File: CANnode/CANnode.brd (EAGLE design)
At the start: 57.9 x 57.7 mm, 247 parts, among them IC1 ISO1050DUB, IC2 ISO1050DUB, Q1 FDV302P, Q3 FDV302P, U1 LM324PW, U10 FT2232HL, U11 93LC56C-I/SN, U2 TPS70445_PWP_24, U3 LM324PW, U4 LM324PW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

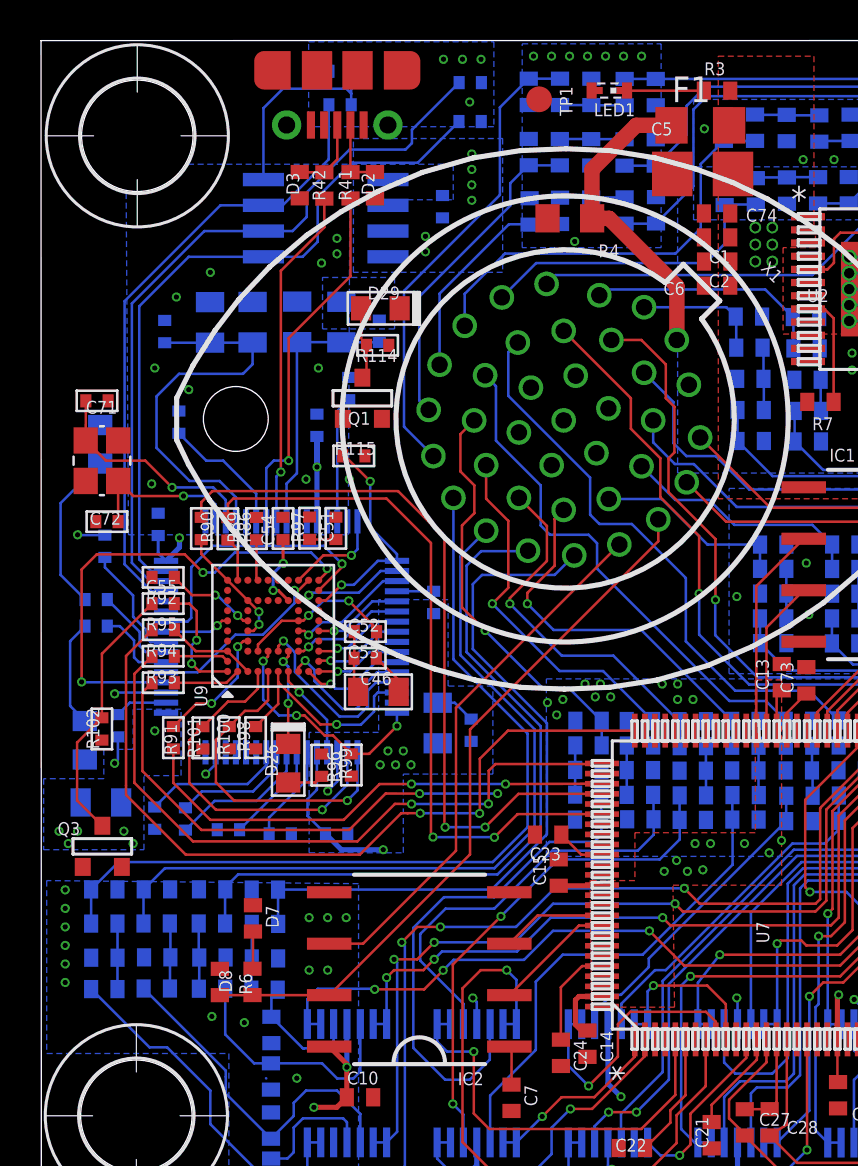
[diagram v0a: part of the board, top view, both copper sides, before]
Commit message: Finished routing bottom layer
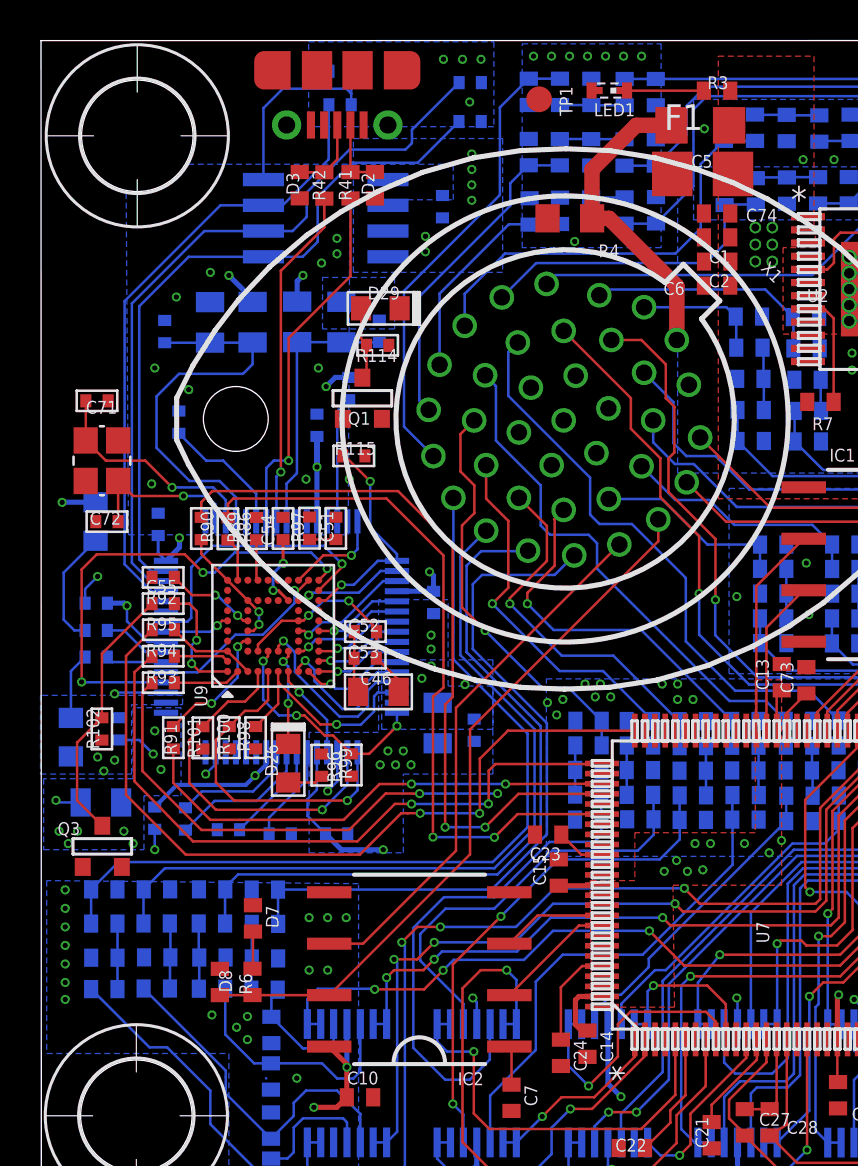
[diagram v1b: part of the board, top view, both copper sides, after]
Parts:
- moved D28 3.82 mm to (10.5, 46.3)
- moved C64 2.84 mm to (10.7, 42.3), turned to 0 degrees
- moved R106 1.52 mm to (10.7, 39.7)
- moved R107 1.52 mm to (10.7, 41.0)
- moved D27 0.70 mm to (9.53, 35.8)
- moved C67 0.17 mm to (11.8, 36.1)
- moved C65 0.15 mm to (29.3, 36.1)
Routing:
- net GND: track 24.4 -> 27.4 mm, vias 95 -> 102
- net N$43: track 8.02 -> 5.82 mm
- net N$42: track 5.30 -> 3.29 mm
- net N$25: track 4.12 -> 3.00 mm
- net N$26: track 4.37 -> 3.34 mm
- net +3V3: track 64.2 -> 65.1 mm, vias 26 -> 39
- net +1V8: vias 11 -> 12

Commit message: Finished grounding and powering. Whole board needs to be reviewed
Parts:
- moved R97 3.05 mm to (24.3, 46.0)
- moved D25 2.55 mm to (57.1, 46.2), turned to 90 degrees
- moved R5 2.43 mm to (57.1, 43.6), turned to 90 degrees
- moved C52 1.77 mm to (25.0, 42.3), turned to 0 degrees
- moved C53 1.56 mm to (25.0, 40.8), turned to 0 degrees
- moved C25 1.39 mm to (53.2, 21.8)
- moved C15 0.89 mm to (33.2, 28.2)
- moved C17 0.78 mm to (54.4, 24.9)
- moved C16 0.76 mm to (48.1, 18.1)
- moved C18 0.76 mm to (53.5, 23.6)
- moved C20 0.75 mm to (53.7, 27.8)
- moved R102 0.70 mm to (10.5, 36.7)
- moved C46 0.57 mm to (24.0, 38.0), turned to 270 degrees
- moved R7 0.37 mm to (46.7, 52.5), turned to 270 degrees
- moved C24 0.25 mm to (33.4, 20.1)
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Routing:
- net GND: track 27.4 -> 95.6 mm, vias 102 -> 137
- net +5V: track 20.3 -> 40.4 mm
- net +3V3: track 65.1 -> 82.9 mm, vias 39 -> 59
- net A3_3V3: track 13.9 -> 20.3 mm
- net POWERGOOD: track 1.30 -> 5.48 mm
- net CAN2L: track 28.5 -> 32.5 mm
- net CAN1L: track 20.1 -> 22.7 mm
- net +1V2: track 12.3 -> 13.8 mm
- net D4_BUFFERED: track 13.9 -> 14.9 mm
- net A11_3V3: track 46.4 -> 47.2 mm
- net A14_BUFFERED: track 19.2 -> 18.4 mm
- net N$12: track 5.59 -> 4.85 mm
- added copper zone on layer 1, net GND

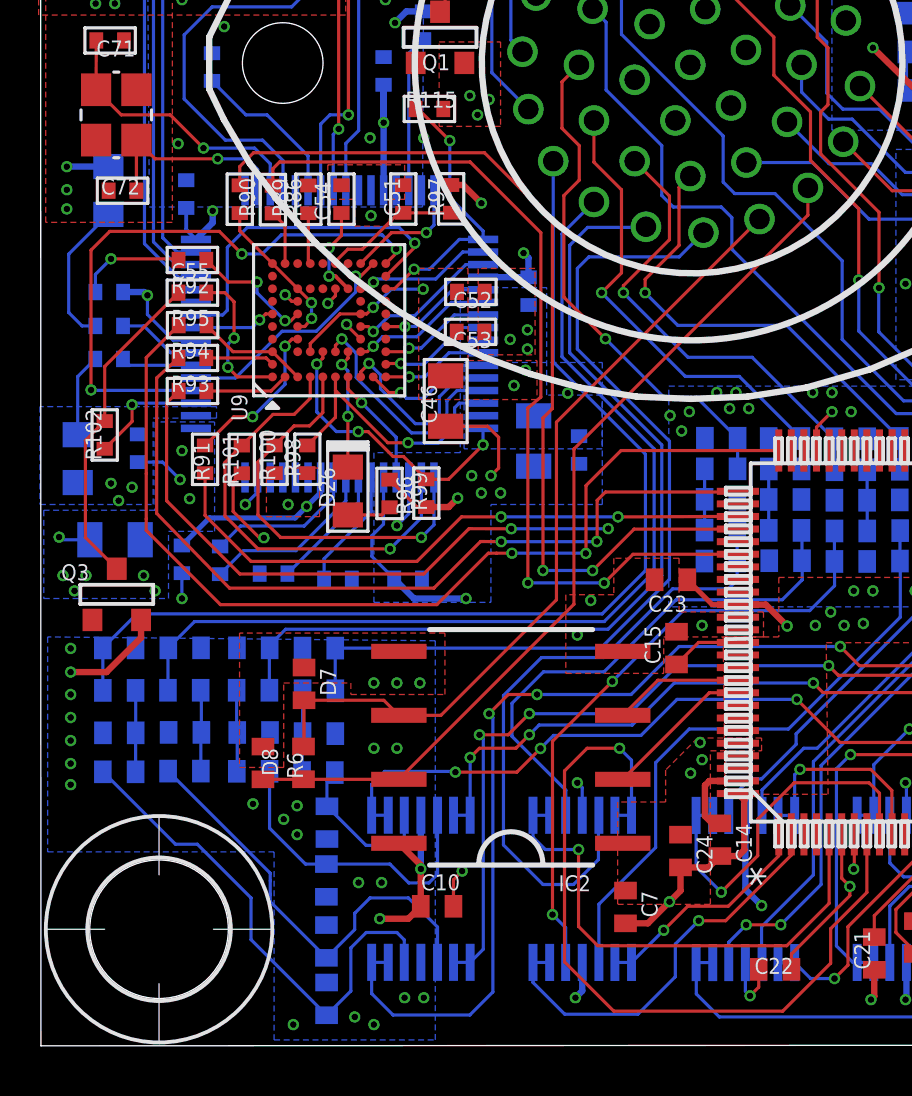
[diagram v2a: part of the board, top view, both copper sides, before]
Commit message: Routed missing JTAG to MCU connections
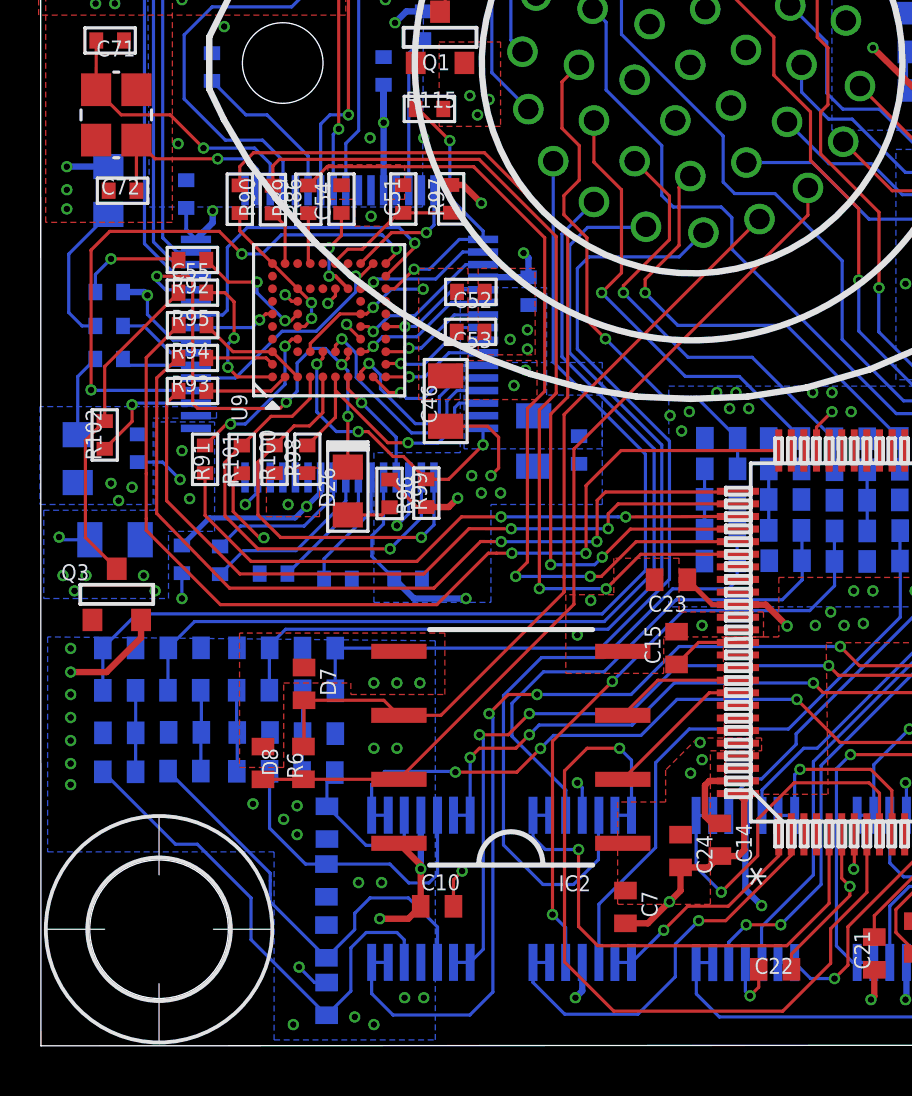
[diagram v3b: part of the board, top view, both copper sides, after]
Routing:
- net MCU_RTCK: track 0.00 -> 34.2 mm, vias 0 -> 2
- net POWER_EN: track 4.79 -> 20.9 mm, vias 2 -> 4
- net MCU_TDI: track 24.1 -> 30.0 mm
- net GND: track 95.6 -> 97.0 mm, vias 137 -> 138
- net MCU_RESET: track 35.5 -> 36.1 mm
- net +3V3: vias 59 -> 58

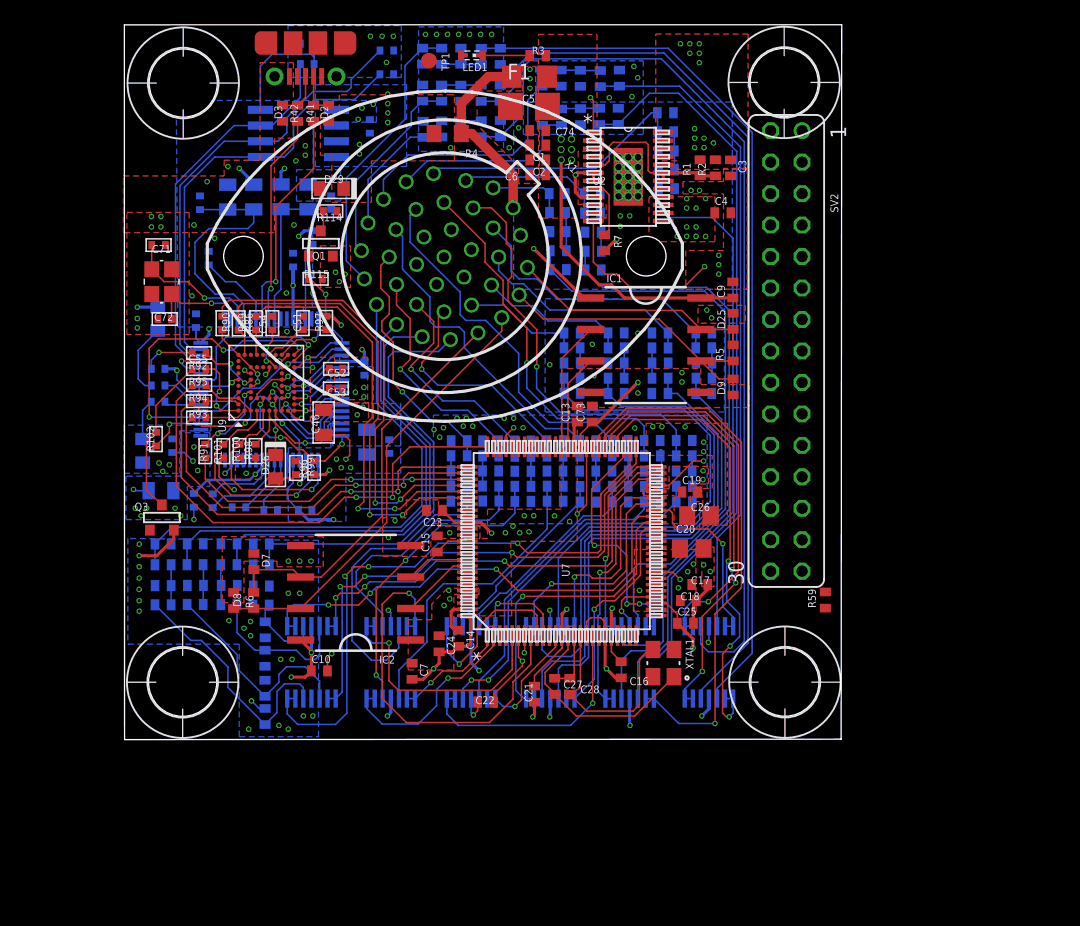
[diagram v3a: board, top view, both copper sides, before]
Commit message: Changed mounting holes to big vias. Move the origin of the board.
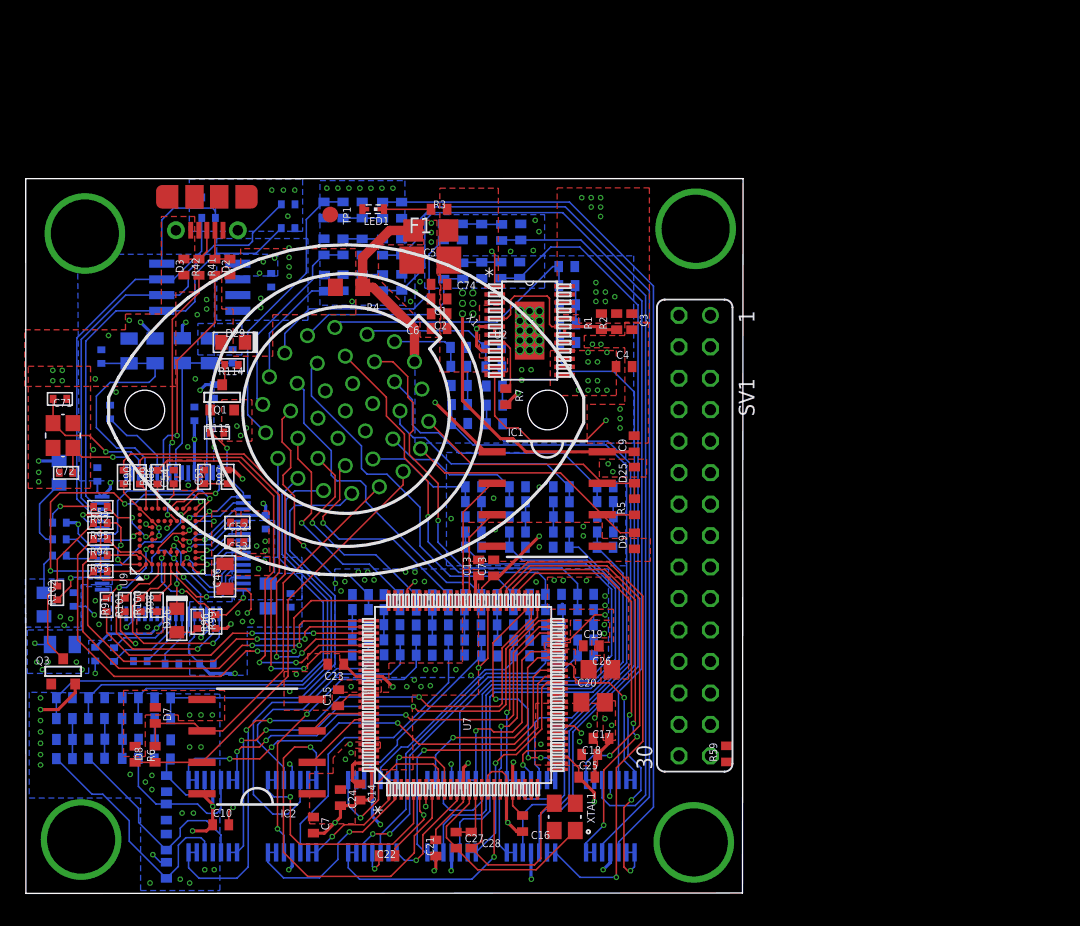
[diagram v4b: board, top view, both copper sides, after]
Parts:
- removed H1, H2, H3, H4: MOUNT-HOLE5.5, holes:5,5
- removed SV2: (no value), con-lsta:FE15-2
- added SV1: (no value), con-lsta:FE15-2
- moved R72 14.8 mm to (25.6, 52.2)
- moved C49 14.8 mm to (36.8, 53.4)
- moved R108 14.8 mm to (14.7, 54.5)
- moved R18 14.8 mm to (28.8, 52.2)
- moved R81 14.8 mm to (36.1, 31.6)
- moved TP1 14.8 mm to (24.6, 54.8)
- moved C2 14.8 mm to (33.4, 46.8)
- moved C21 14.8 mm to (33.1, 3.67)
- moved C26 14.8 mm to (46.4, 18.1)
- moved C3 14.8 mm to (48.9, 46.2)
- moved C33 14.8 mm to (40.0, 21.7)
- moved C4 14.8 mm to (48.3, 42.5)
- moved C44 14.8 mm to (45.2, 21.7)
- moved C48 14.8 mm to (35.0, 41.0)
- moved C73 14.8 mm to (37.8, 26.3)
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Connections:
- net +1V2: now also SV1.28; no longer SV2.28
- net +3V3: now also SV1.30; no longer SV2.30
- net +5V: now also SV1.29; no longer SV2.29
- net 5V_IN: now also SV1.27
- net A0_IN: now also SV1.15
- net A10_IN: now also SV1.22
- net A11_IN: now also SV1.20
- net A12_IN: now also SV1.18
- net A1_IN: now also SV1.13
- net A2_IN: now also SV1.11
- net A3_IN: now also SV1.9
- net A4_IN: now also SV1.7
- net A5_IN: now also SV1.5
- net A6_IN: now also SV1.3
- net A7_IN: now also SV1.1; no longer SV2.1
- net A8_IN: now also SV1.26
- net A9_IN: now also SV1.24
- net CAN1RX: now also SV1.23
- net CAN1TX: now also SV1.21
- net CAN2RX: now also SV1.19
- net CAN2TX: now also SV1.17
- net D0_IN: now also SV1.16
- net D1_IN: now also SV1.14
- net D2_IN: now also SV1.12
- net D3_IN: now also SV1.10
- net D4_IN: now also SV1.8
- net D5_IN: now also SV1.6
- net D6_IN: now also SV1.4
- net D7_IN: now also SV1.2; no longer SV2.2
- net GND: now also SV1.25

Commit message: added connector
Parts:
- added X2: 1751316, con-phoenix-350:1751316

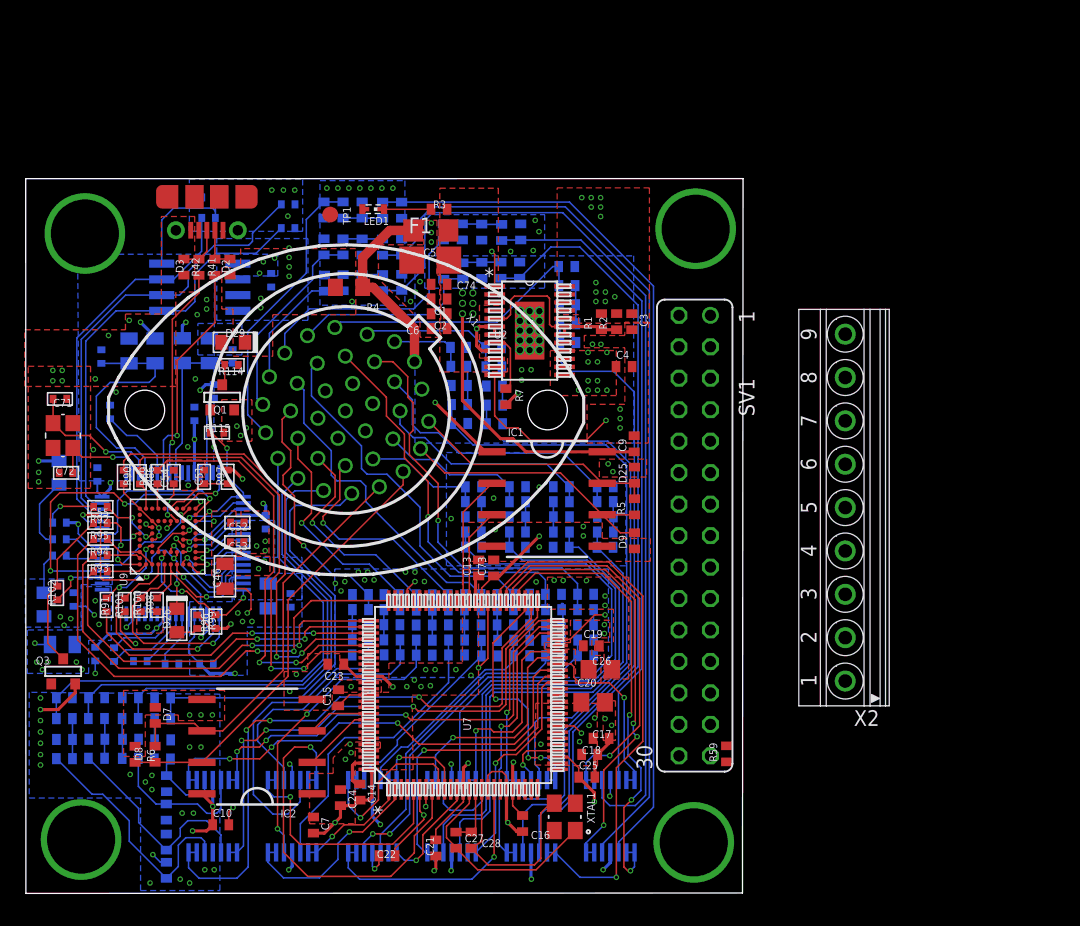
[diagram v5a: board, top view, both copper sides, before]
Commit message: Started routing Debug headers
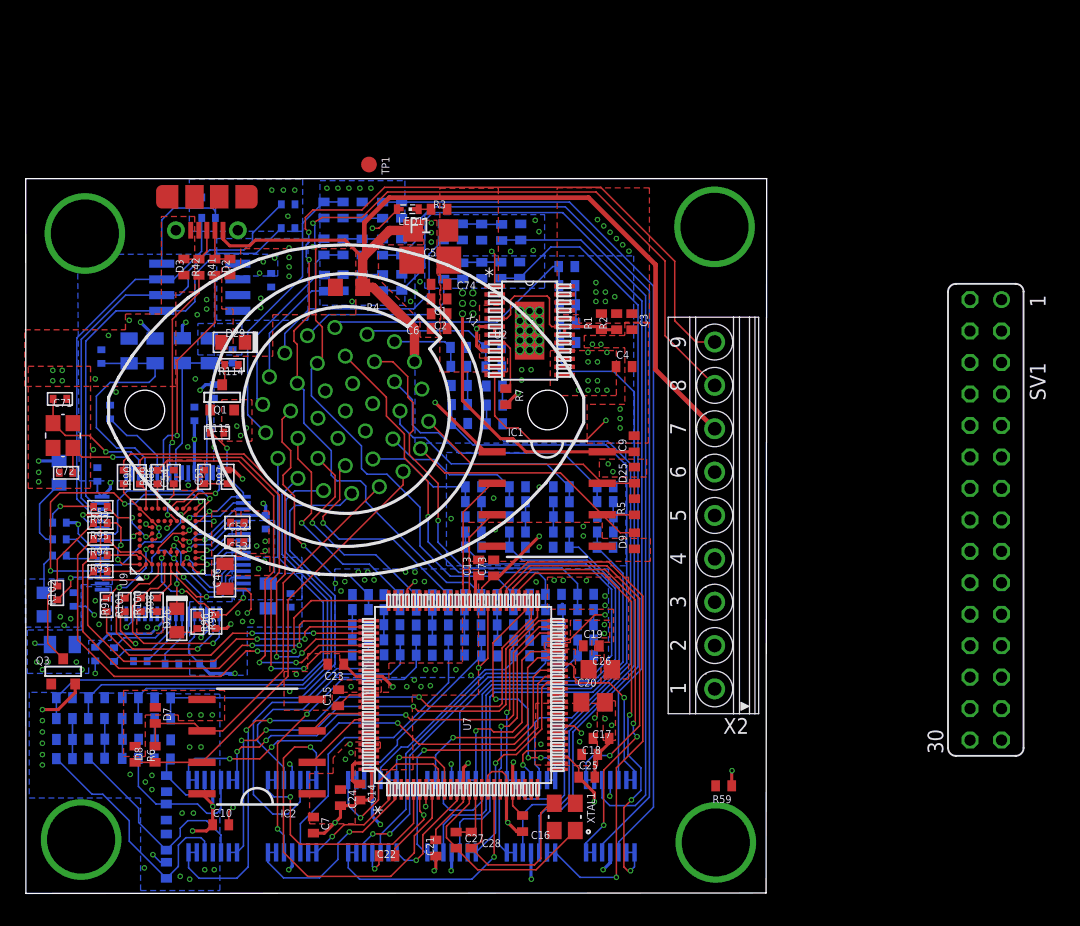
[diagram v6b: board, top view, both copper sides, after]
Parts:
- moved SV1 23.5 mm to (77.5, 30.2)
- moved X2 10.6 mm to (55.5, 30.5)
- moved TP1 5.11 mm to (27.7, 58.8)
- moved LED1 2.79 mm to (30.8, 55.2)
- moved R59 2.59 mm to (56.3, 8.69), turned to 180 degrees
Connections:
- new net N$44: X2.6
- new net N$69: X2.5
- new net N$70: X2.4
- new net N$71: X2.3
- new net N$72: X2.2
- net +1V2: no longer SV1.28
- net +3V3: no longer SV1.30
- net +5V: no longer SV1.29
- net 5V_IN: now also X2.7; no longer SV1.27
- net A0_IN: no longer SV1.15
- net A10_IN: no longer SV1.22
- net A11_IN: no longer SV1.20
- net A12_IN: no longer SV1.18
- net A1_IN: no longer SV1.13
- net A2_IN: no longer SV1.11
- net A3_IN: no longer SV1.9
- net A4_IN: no longer SV1.7
- net A5_IN: no longer SV1.5
- net A6_IN: no longer SV1.3
- net A7_IN: no longer SV1.1
- net A8_IN: no longer SV1.26
- net A9_IN: no longer SV1.24
- net CAN1RX: no longer SV1.23
- net CAN1TX: no longer SV1.21
- net CAN2RX: no longer SV1.19
- net CAN2TX: no longer SV1.17
- net D0_IN: no longer SV1.16
- net D1_IN: no longer SV1.14
- net D2_IN: no longer SV1.12
- net D3_IN: no longer SV1.10
- net D4_IN: now also X2.9; no longer SV1.8
- net D5_IN: now also X2.8; no longer SV1.6
- net D6_IN: no longer SV1.4
- net D7_IN: no longer SV1.2
- net GND: now also X2.1; no longer SV1.25
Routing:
- net 5V_IN: track 15.6 -> 73.6 mm
- net D4_IN: track 26.6 -> 82.9 mm, vias 0 -> 2
- net D5_IN: track 29.9 -> 85.3 mm, vias 0 -> 2
- net GND: track 97.0 -> 101.2 mm, vias 138 -> 137
- net N$2: track 4.17 -> 1.38 mm
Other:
- board size 57.9 x 57.7 mm -> 59.8 x 57.7 mm
